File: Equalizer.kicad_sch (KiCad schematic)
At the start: 37 parts, among them U201 TL072, U202 TL074, U203 TL074

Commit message: 回路図ひとまず完成
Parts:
- renumbered C215 to C301, C213 to C302, C214 to C303, C201 to C304, C205 to C305, C209 to C306, C203 to C307, C207 to C308, C211 to C309, C202 to C310, C206 to C311, C210 to C312, C204 to C313, C208 to C314, C212 to C315, R215 to R301, R201 to R302, R203 to R303, R207 to R304, R211 to R305, R205 to R306, R209 to R307, R213 to R308, R216 to R309, R202 to R310, R204 to R311, R208 to R312, R212 to R313, R206 to R314, R210 to R315, R214 to R316, RV201 to RV301, RV202 to RV302, RV203 to RV303, U201 to U301, U202 to U302, U203 to U303
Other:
- note added: "600Hz"
- note added: "60Hz"
- note added: "6kHz"
- note removed: "100Hz"
- note removed: "10kHz"
- note removed: "1kHz"

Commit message: 部品ほぼ割り当て
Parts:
- C301, C302, C303: footprint (none) -> Capacitor_SMD:C_1206_3216Metric
- R301, R302, R303, R304, R305, R306, R307, R308, R309, R310, R311, R312, R313, R314, R315, R316: footprint Resistor_THT:R_Axial_DIN0204_L3.6mm_D1.6mm_P5.08mm_Horizontal -> Resistor_SMD:R_0603_1608Metric
- RV301, RV302, RV303: footprint MyLibrary:SL4515G -> MyLibrary:RV_2C
- U301: footprint (none) -> Package_DIP:DIP-8_W7.62mm_Socket
- U302, U303: footprint (none) -> Package_DIP:DIP-14_W7.62mm_Socket
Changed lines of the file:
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@@
 			)
 		)
-		(property "Footprint" ""
+		(property "Footprint" "Package_DIP:DIP-8_W7.62mm_Socket"
 			(at 237.49 25.4 0)
 			(hide yes)
@@
 			)
 		)
-		(property "Footprint" "Resistor_THT:R_Axial_DIN0204_L3.6mm_D1.6mm_P5.08mm_Horizontal"
+		(property "Footprint" "Resistor_SMD:R_0603_1608Metric"
 			(at 145.288 71.12 90)
 			(hide yes)
@@
 			)
 		)
-		(property "Footprint" "Resistor_THT:R_Axial_DIN0204_L3.6mm_D1.6mm_P5.08mm_Horizontal"
+		(property "Footprint" "Resistor_SMD:R_0603_1608Metric"
 			(at 179.832 134.62 90)
 			(hide yes)
@@
 			)
 		)
-		(property "Footprint" "Resistor_THT:R_Axial_DIN0204_L3.6mm_D1.6mm_P5.08mm_Horizontal"
+		(property "Footprint" "Resistor_SMD:R_0603_1608Metric"
 			(at 145.288 127 90)
 			(hide yes)
@@
 			)
 		)
-		(property "Footprint" "Resistor_THT:R_Axial_DIN0204_L3.6mm_D1.6mm_P5.08mm_Horizontal"
+		(property "Footprint" "Resistor_SMD:R_0603_1608Metric"
 			(at 110.49 60.198 90)
 			(hide yes)
@@
 			)
 		)
-		(property "Footprint" "Resistor_THT:R_Axial_DIN0204_L3.6mm_D1.6mm_P5.08mm_Horizontal"
+		(property "Footprint" "Resistor_SMD:R_0603_1608Metric"
 			(at 189.23 50.038 90)
 			(hide yes)
@@
 			)
 		)
-		(property "Footprint" ""
+		(property "Footprint" "Package_DIP:DIP-14_W7.62mm_Socket"
 			(at 173.99 138.43 0)
 			(hide yes)
@@
 			)
 		)
-		(property "Footprint" "MyLibrary:SL4515G"
+		(property "Footprint" "MyLibrary:RV_2C"
 			(at 119.38 110.49 0)
 			(hide yes)
@@
 			)
 		)
-		(property "Footprint" ""
+		(property "Footprint" "Package_DIP:DIP-14_W7.62mm_Socket"
 			(at 146.05 138.43 0)
 			(hide yes)
@@
 			)
 		)
-		(property "Footprint" "Resistor_THT:R_Axial_DIN0204_L3.6mm_D1.6mm_P5.08mm_Horizontal"
+		(property "Footprint" "Resistor_SMD:R_0603_1608Metric"
 			(at 151.892 78.74 90)
 			(hide yes)
@@
 			)
 		)
-		(property "Footprint" "Resistor_THT:R_Axial_DIN0204_L3.6mm_D1.6mm_P5.08mm_Horizontal"
+		(property "Footprint" "Resistor_SMD:R_0603_1608Metric"
 			(at 117.348 71.12 90)
 			(hide yes)
@@
 			)
 		)
-		(property "Footprint" "Resistor_THT:R_Axial_DIN0204_L3.6mm_D1.6mm_P5.08mm_Horizontal"
+		(property "Footprint" "Resistor_SMD:R_0603_1608Metric"
 			(at 173.228 127 90)
 			(hide yes)
@@
 			)
 		)
-		(property "Footprint" ""
+		(property "Footprint" "Package_DIP:DIP-14_W7.62mm_Socket"
 			(at 118.11 82.55 0)
 			(hide yes)
@@
 			)
 		)
-		(property "Footprint" ""
+		(property "Footprint" "Package_DIP:DIP-14_W7.62mm_Socket"
 			(at 273.05 25.4 0)
 			(hide yes)
@@
 			)
 		)
-		(property "Footprint" "Resistor_THT:R_Axial_DIN0204_L3.6mm_D1.6mm_P5.08mm_Horizontal"
+		(property "Footprint" "Resistor_SMD:R_0603_1608Metric"
 			(at 151.892 134.62 90)
 			(hide yes)
@@
 			)
 		)
-		(property "Footprint" ""
+		(property "Footprint" "Package_DIP:DIP-14_W7.62mm_Socket"
 			(at 173.99 82.55 0)
 			(hide yes)
@@
 			)
 		)
-		(property "Footprint" ""
+		(property "Footprint" "Package_DIP:DIP-14_W7.62mm_Socket"
 			(at 146.05 82.55 0)
 			(hide yes)
@@
 			)
 		)
-		(property "Footprint" "Resistor_THT:R_Axial_DIN0204_L3.6mm_D1.6mm_P5.08mm_Horizontal"
+		(property "Footprint" "Resistor_SMD:R_0603_1608Metric"
 			(at 117.348 127 90)
 			(hide yes)
@@
 			)
 		)
-		(property "Footprint" "MyLibrary:SL4515G"
+		(property "Footprint" "MyLibrary:RV_2C"
 			(at 147.32 110.49 0)
 			(hide yes)
@@
 			)
 		)
-		(property "Footprint" ""
+		(property "Footprint" "Capacitor_SMD:C_1206_3216Metric"
 			(at 272.7452 29.21 0)
 			(hide yes)
@@
 			)
 		)
-		(property "Footprint" "Resistor_THT:R_Axial_DIN0204_L3.6mm_D1.6mm_P5.08mm_Horizontal"
+		(property "Footprint" "Resistor_SMD:R_0603_1608Metric"
 			(at 123.952 78.74 90)
 			(hide yes)
@@
 			)
 		)
-		(property "Footprint" "Resistor_THT:R_Axial_DIN0204_L3.6mm_D1.6mm_P5.08mm_Horizontal"
+		(property "Footprint" "Resistor_SMD:R_0603_1608Metric"
 			(at 110.49 116.078 90)
 			(hide yes)
@@
 			)
 		)
-		(property "Footprint" "Resistor_THT:R_Axial_DIN0204_L3.6mm_D1.6mm_P5.08mm_Horizontal"
+		(property "Footprint" "Resistor_SMD:R_0603_1608Metric"
 			(at 173.228 71.12 90)
 			(hide yes)
@@
 			)
 		)
-		(property "Footprint" "Resistor_THT:R_Axial_DIN0204_L3.6mm_D1.6mm_P5.08mm_Horizontal"
+		(property "Footprint" "Resistor_SMD:R_0603_1608Metric"
 			(at 179.832 78.74 90)
 			(hide yes)
@@
 			)
 		)
-		(property "Footprint" ""
+		(property "Footprint" "Package_DIP:DIP-14_W7.62mm_Socket"
 			(at 189.23 54.61 0)
 			(hide yes)
@@
 			)
 		)
-		(property "Footprint" ""
+		(property "Footprint" "Package_DIP:DIP-8_W7.62mm_Socket"
 			(at 93.98 58.42 0)
 			(hide yes)
@@
 			)
 		)
-		(property "Footprint" ""
+		(property "Footprint" "Package_DIP:DIP-14_W7.62mm_Socket"
 			(at 252.73 25.4 0)
 			(hide yes)
@@
 			)
 		)
-		(property "Footprint" ""
+		(property "Footprint" "Capacitor_SMD:C_1206_3216Metric"
 			(at 252.4252 29.21 0)
 			(hide yes)
@@
 			)
 		)
-		(property "Footprint" "Resistor_THT:R_Axial_DIN0204_L3.6mm_D1.6mm_P5.08mm_Horizontal"
+		(property "Footprint" "Resistor_SMD:R_0603_1608Metric"
 			(at 123.952 134.62 90)
 			(hide yes)
@@
 			)
 		)
-		(property "Footprint" ""
+		(property "Footprint" "Package_DIP:DIP-8_W7.62mm_Socket"
 			(at 93.98 114.3 0)
 			(hide yes)
@@
 			)
 		)
-		(property "Footprint" "Resistor_THT:R_Axial_DIN0204_L3.6mm_D1.6mm_P5.08mm_Horizontal"
+		(property "Footprint" "Resistor_SMD:R_0603_1608Metric"
 			(at 189.23 105.918 90)
 			(hide yes)
@@
 			)
 		)
-		(property "Footprint" "MyLibrary:SL4515G"
+		(property "Footprint" "MyLibrary:RV_2C"
 			(at 147.32 54.61 0)
 			(hide yes)
@@
 			)
 		)
-		(property "Footprint" "MyLibrary:SL4515G"
+		(property "Footprint" "MyLibrary:RV_2C"
 			(at 175.26 110.49 0)
 			(hide yes)
@@
 			)
 		)
-		(property "Footprint" "MyLibrary:SL4515G"
+		(property "Footprint" "MyLibrary:RV_2C"
 			(at 175.26 54.61 0)
 			(hide yes)
@@
 			)
 		)
-		(property "Footprint" ""
+		(property "Footprint" "Package_DIP:DIP-14_W7.62mm_Socket"
 			(at 118.11 138.43 0)
 			(hide yes)
@@
 			)
 		)
-		(property "Footprint" ""
+		(property "Footprint" "Package_DIP:DIP-14_W7.62mm_Socket"
 			(at 189.23 110.49 0)
 			(hide yes)
@@
 			)
 		)
-		(property "Footprint" "MyLibrary:SL4515G"
+		(property "Footprint" "MyLibrary:RV_2C"
 			(at 119.38 54.61 0)
 			(hide yes)
@@
 			)
 		)
-		(property "Footprint" ""
+		(property "Footprint" "Capacitor_SMD:C_1206_3216Metric"
 			(at 232.1052 29.21 0)
 			(hide yes)

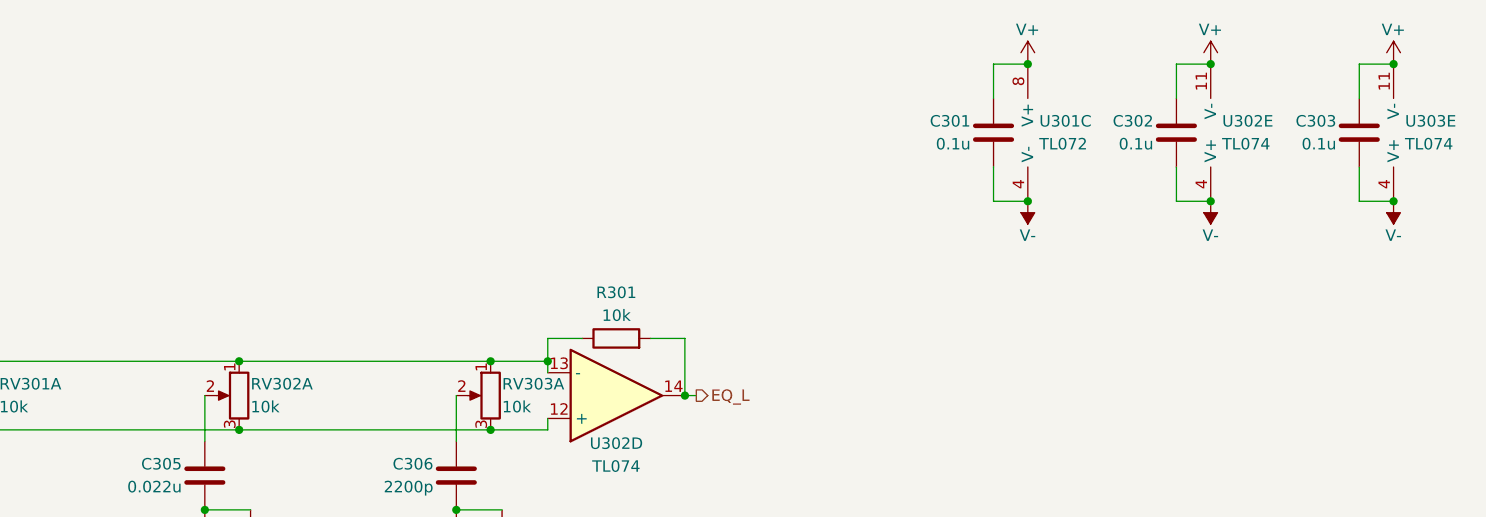
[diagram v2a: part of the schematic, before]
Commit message: 回路図一部変更，部品ほぼ置いた　寝かせる
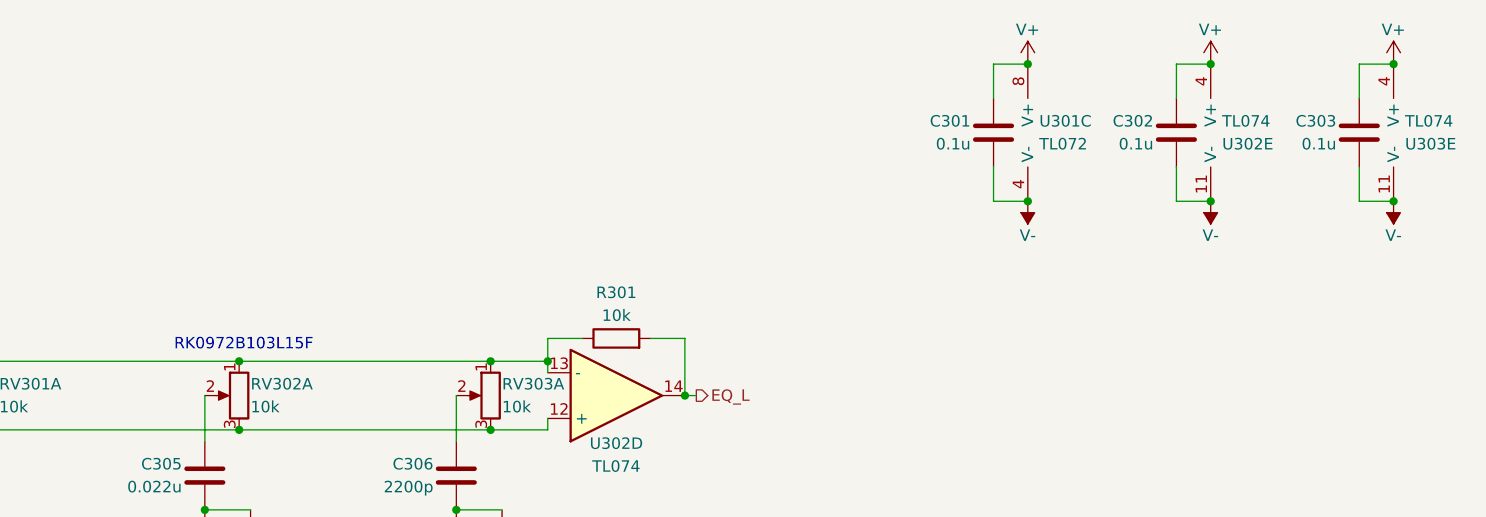
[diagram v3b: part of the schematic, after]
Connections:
- net V+: now also U302.4 (V+), U303.4 (V+); no longer U302.11 (V-), U303.11 (V-)
- net V-: now also U302.11 (V-), U303.11 (V-); no longer U302.4 (V+), U303.4 (V+)
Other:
- note added: "RK0972B103L15F"
- moved on the sheet: U302E, U303E
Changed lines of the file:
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@@
 		)
 	)
+	(text "RK0972B103L15F"
+		(exclude_from_sim no)
+		(at 147.828 49.022 0)
+		(effects
+			(font
+				(size 1.27 1.27)
+			)
+			(href "https://akizukidenshi.com/catalog/g/g112576/")
+		)
+	)
 	(text "6kHz"
 		(exclude_from_sim no)
@@
 	)
 	(junction
-		(at 120.65 130.81)
+		(at 255.27 17.78)
 		(diameter 0)
 		(color 0 0 0 0)
 	)
 	(junction
-		(at 175.26 114.3)
+		(at 120.65 130.81)
 		(diameter 0)
 		(color 0 0 0 0)
 	)
 	(junction
-		(at 255.27 33.02)
+		(at 175.26 114.3)
 		(diameter 0)
 		(color 0 0 0 0)
@@
 	)
 	(junction
-		(at 255.27 17.78)
-		(diameter 0)
-		(color 0 0 0 0)
-	)
-	(junction
 		(at 275.59 17.78)
 		(diameter 0)
@@
 	)
 	(junction
+		(at 255.27 33.02)
+		(diameter 0)
+		(color 0 0 0 0)
+	)
+	(junction
 		(at 115.57 67.31)
 		(diameter 0)
@@
 	(symbol
 		(lib_id "Device:Opamp_Quad")
-		(at 273.05 25.4 180)
+		(at 273.05 25.4 0)
+		(mirror y)
 		(unit 5)
 		(body_style 1)
@@
 		(dnp no)
 		(property "Reference" "U303"
-			(at 276.86 24.1299 0)
+			(at 276.86 26.6701 0)
 			(show_name no)
 			(do_not_autoplace no)
@@
 		)
 		(property "Value" "TL074"
-			(at 276.86 26.6699 0)
+			(at 276.86 24.1301 0)
 			(show_name no)
 			(do_not_autoplace no)
@@
 	(symbol
 		(lib_id "Device:Opamp_Quad")
-		(at 252.73 25.4 180)
+		(at 252.73 25.4 0)
+		(mirror y)
 		(unit 5)
 		(body_style 1)
@@
 		(dnp no)
 		(property "Reference" "U302"
-			(at 256.54 24.1299 0)
+			(at 256.54 26.6701 0)
 			(show_name no)
 			(do_not_autoplace no)
@@
 		)
 		(property "Value" "TL074"
-			(at 256.54 26.6699 0)
+			(at 256.54 24.1301 0)
 			(show_name no)
 			(do_not_autoplace no)

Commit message: 部品配置進行中
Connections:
- net SIG_L: now also U301.5 (+); no longer U301.3 (+)
- net SIG_R: now also U301.3 (+); no longer U301.5 (+)
- net at U301.1, U301.2 (-): now also R310.1; no longer R302.1
- net at U301.6 (-), U301.7: now also R302.1; no longer R310.1
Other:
- moved on the sheet: U301A, U301B
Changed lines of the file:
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@@
 	)
 	(junction
-		(at 101.6 114.3)
+		(at 115.57 74.93)
 		(diameter 0)
 		(color 0 0 0 0)
 	)
 	(junction
-		(at 115.57 74.93)
+		(at 176.53 74.93)
 		(diameter 0)
 		(color 0 0 0 0)
 	)
 	(junction
-		(at 176.53 74.93)
+		(at 171.45 74.93)
 		(diameter 0)
 		(color 0 0 0 0)
 	)
 	(junction
-		(at 171.45 74.93)
+		(at 101.6 114.3)
 		(diameter 0)
 		(color 0 0 0 0)
@@
 	)
 	(junction
-		(at 148.59 74.93)
+		(at 101.6 58.42)
 		(diameter 0)
 		(color 0 0 0 0)
 	)
 	(junction
-		(at 148.59 130.81)
+		(at 148.59 74.93)
 		(diameter 0)
 		(color 0 0 0 0)
 	)
 	(junction
-		(at 101.6 58.42)
+		(at 148.59 130.81)
 		(diameter 0)
 		(color 0 0 0 0)
@@
 	(symbol
 		(lib_id "Device:Opamp_Dual")
-		(at 93.98 58.42 0)
+		(at 93.98 114.3 0)
 		(unit 1)
 		(body_style 1)
@@
 		(dnp no)
 		(property "Reference" "U301"
-			(at 93.98 50.8 0)
+			(at 93.98 106.68 0)
 			(show_name no)
 			(do_not_autoplace no)
@@
 		)
 		(property "Value" "TL072"
-			(at 93.98 53.34 0)
+			(at 93.98 109.22 0)
 			(show_name no)
 			(do_not_autoplace no)
@@
 		)
 		(property "Footprint" "Package_DIP:DIP-8_W7.62mm_Socket"
-			(at 93.98 58.42 0)
+			(at 93.98 114.3 0)
 			(hide yes)
 			(show_name no)
@@
 		)
 		(property "Datasheet" ""
-			(at 93.98 58.42 0)
+			(at 93.98 114.3 0)
 			(hide yes)
 			(show_name no)
@@
 		)
 		(property "Description" "Dual operational amplifier"
-			(at 93.98 58.42 0)
+			(at 93.98 114.3 0)
 			(hide yes)
 			(show_name no)
@@
 		)
 		(property "Sim.Library" "${KICAD9_SYMBOL_DIR}/Simulation_SPICE.sp"
-			(at 93.98 58.42 0)
+			(at 93.98 114.3 0)
 			(hide yes)
 			(show_name no)
@@
 		)
 		(property "Sim.Name" "kicad_builtin_opamp_dual"
-			(at 93.98 58.42 0)
+			(at 93.98 114.3 0)
 			(hide yes)
 			(show_name no)
@@
 		)
 		(property "Sim.Device" "SUBCKT"
-			(at 93.98 58.42 0)
+			(at 93.98 114.3 0)
 			(hide yes)
 			(show_name no)
@@
 		)
 		(property "Sim.Pins" "1=out1 2=in1- 3=in1+ 4=vee 5=in2+ 6=in2- 7=out2 8=vcc"
-			(at 93.98 58.42 0)
+			(at 93.98 114.3 0)
 			(hide yes)
 			(show_name no)
@@
 	(symbol
 		(lib_id "Device:Opamp_Dual")
-		(at 93.98 114.3 0)
+		(at 93.98 58.42 0)
 		(unit 2)
 		(body_style 1)
@@
 		(dnp no)
 		(property "Reference" "U301"
-			(at 93.98 106.68 0)
+			(at 93.98 50.8 0)
 			(show_name no)
 			(do_not_autoplace no)
@@
 		)
 		(property "Value" "TL072"
-			(at 93.98 109.22 0)
+			(at 93.98 53.34 0)
 			(show_name no)
 			(do_not_autoplace no)
@@
 		)
 		(property "Footprint" "Package_DIP:DIP-8_W7.62mm_Socket"
-			(at 93.98 114.3 0)
+			(at 93.98 58.42 0)
 			(hide yes)
 			(show_name no)
@@
 		)
 		(property "Datasheet" ""
-			(at 93.98 114.3 0)
+			(at 93.98 58.42 0)
 			(hide yes)
 			(show_name no)
@@
 		)
 		(property "Description" "Dual operational amplifier"
-			(at 93.98 114.3 0)
+			(at 93.98 58.42 0)
 			(hide yes)
 			(show_name no)
@@
 		)
 		(property "Sim.Library" "${KICAD9_SYMBOL_DIR}/Simulation_SPICE.sp"
-			(at 93.98 114.3 0)
+			(at 93.98 58.42 0)
 			(hide yes)
 			(show_name no)
@@
 		)
 		(property "Sim.Name" "kicad_builtin_opamp_dual"
-			(at 93.98 114.3 0)
+			(at 93.98 58.42 0)
 			(hide yes)
 			(show_name no)
@@
 		)
 		(property "Sim.Device" "SUBCKT"
-			(at 93.98 114.3 0)
+			(at 93.98 58.42 0)
 			(hide yes)
 			(show_name no)
@@
 		)
 		(property "Sim.Pins" "1=out1 2=in1- 3=in1+ 4=vee 5=in2+ 6=in2- 7=out2 8=vcc"
-			(at 93.98 114.3 0)
+			(at 93.98 58.42 0)
 			(hide yes)
 			(show_name no)
